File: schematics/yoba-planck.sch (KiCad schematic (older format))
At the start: 106 parts, among them M1 AUDIO-JACK3, M2 AUDIO-JACK3, M3 ARDUINO_PRO_MICRO, Q1 BS170, SW1 SW_PUSH, SW10 SW_PUSH, SW11 SW_PUSH, SW12 SW_PUSH, SW13 SW_PUSH, SW14 SW_PUSH, SW15 SW_PUSH, SW16 SW_PUSH, SW17 SW_PUSH, SW18 SW_PUSH, SW19 SW_PUSH, SW2 SW_PUSH, SW20 SW_PUSH, SW21 SW_PUSH, SW22 SW_PUSH, SW23 SW_PUSH, SW24 SW_PUSH, SW3 SW_PUSH, SW4 SW_PUSH, SW5 SW_PUSH, SW6 SW_PUSH, SW7 SW_PUSH, SW8 SW_PUSH, SW9 SW_PUSH

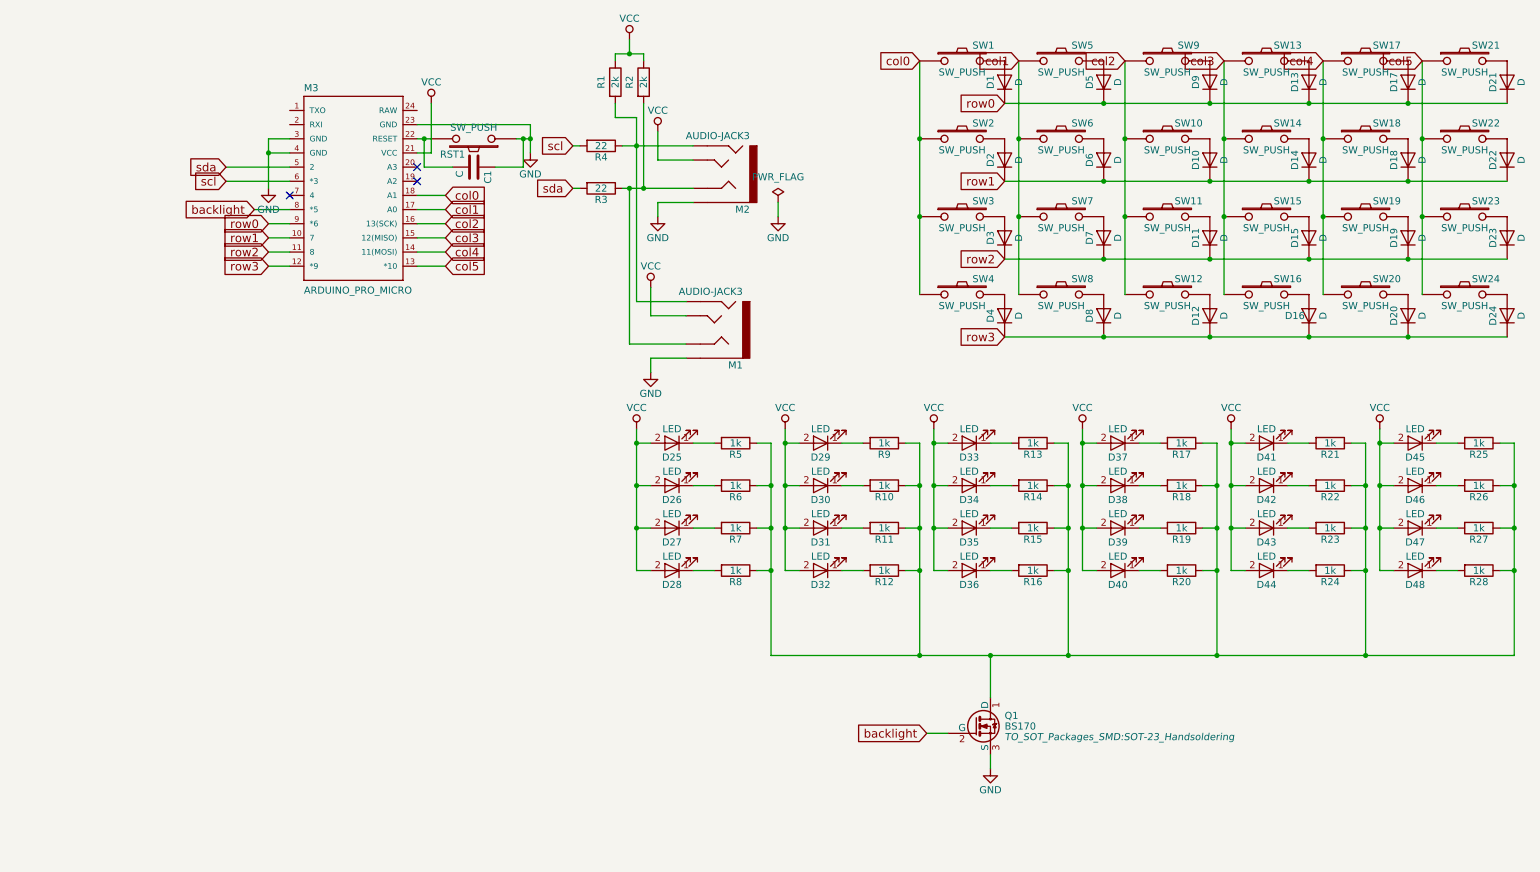
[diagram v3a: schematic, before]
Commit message: yoba rev3 to smd
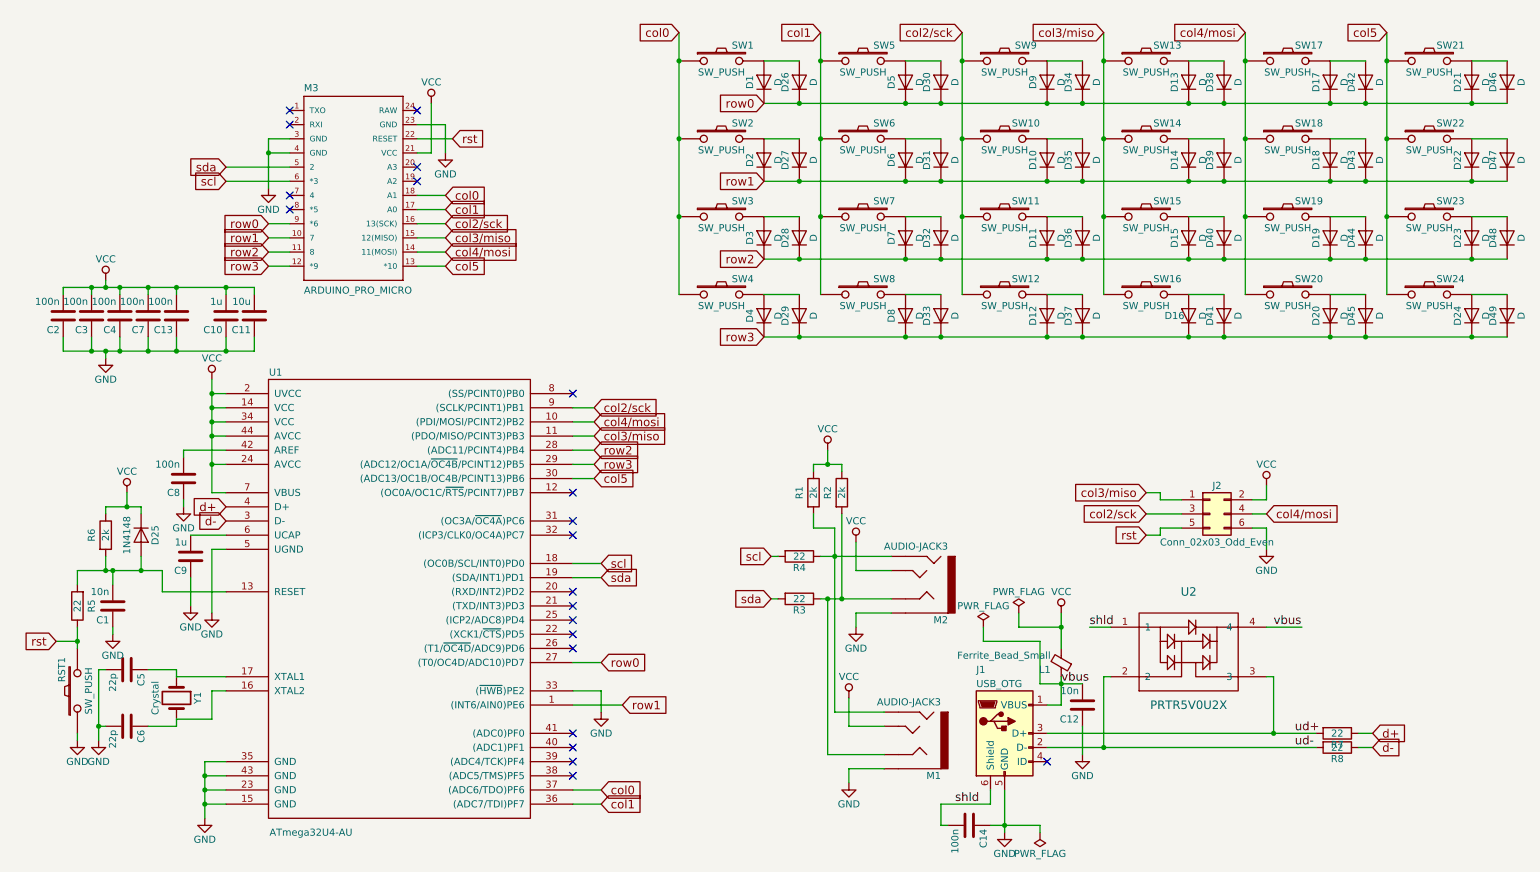
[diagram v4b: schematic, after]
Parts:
- removed D25, D26, D27, D28, D29, D30, D31, D32, D33, D34, D35, D36, D37, D38, D39, D40, D41, D42, D43, D44, D45, D46, D47, D48: LED, mx1a:MX1A-led, symbol LED
- removed Q1: BS170, TO_SOT_Packages_SMD:SOT-23_Handsoldering, symbol BS170
- removed R10, R11, R12, R13, R14, R15, R16, R17, R18, R19, R20, R21, R22, R23, R24, R25, R26, R27, R28, R9: 1k, Resistors_SMD:R_0805_HandSoldering, symbol R
- added C10, C9: 1u, Capacitors_SMD:C_0603_HandSoldering, symbol C
- added C11: 10u, Capacitors_SMD:C_0805_HandSoldering, symbol C
- added C12: 10n, Capacitors_SMD:C_0603_HandSoldering, symbol C
- added C13, C14, C2, C3, C4, C7, C8: 100n, Capacitors_SMD:C_0603_HandSoldering, symbol C
- added C5, C6: 22p, Capacitors_SMD:C_0603_HandSoldering, symbol C
- added D25: 1N4148, Diodes_SMD:SOD-123, symbol D
- added D26, D27, D28, D29, D30, D31, D32, D33, D34, D35, D36, D37, D38, D39, D40, D41, D42, D43, D44, D45, D46, D47, D48, D49: D, Diodes_SMD:SOD-123, symbol D
- added J1: USB_OTG, Connect:USB_Micro-B_10103594-0001LF, symbol USB_OTG
- added J2: Conn_02x03_Odd_Even, Pin_Headers:Pin_Header_Straight_2x03, symbol Conn_02x03_Odd_Even
- added L1: Ferrite_Bead_Small, Capacitors_SMD:C_0603_HandSoldering, symbol Ferrite_Bead_Small
- added U1: ATmega32U4-AU, Housings_QFP:TQFP-44_10x10mm_Pitch0.8mm, symbol ATmega32U4-AU
- added U2: PRTR5V0U2X, yoba:SOT143B, symbol PRTR5V0U2X
- added Y1: Crystal, Crystals:Crystal_SMD_5032_2Pads, symbol Crystal
- C1: value C -> 10n; footprint Capacitors_SMD:C_0805_HandSoldering -> Capacitors_SMD:C_0603_HandSoldering
- R1, R2, R3, R4: footprint Resistors_SMD:R_0805_HandSoldering -> Resistors_Universal:Resistor_SMDuniversal_0805to1206_HandSoldering
- R5, R7, R8: value 1k -> 22; footprint Resistors_SMD:R_0805_HandSoldering -> Resistors_SMD:R_0603_HandSoldering
- R6: value 1k -> 2k; footprint Resistors_SMD:R_0805_HandSoldering -> Resistors_SMD:R_0603_HandSoldering
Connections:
- net GND: now also C10.1, C11.1, C12.1, C13.1, C14.1, C2.1, C3.1, C4.1, C5.2, C6.2, C7.1, C8.1, C9.1, J1.5 (GND), J2.6 (Pin_6), U1.15 (GND), U1.23 (GND), U1.33 ((~HWB~)PE2), U1.35 (GND), U1.43 (GND), U1.5 (UGND)
- net VCC: now also R6.1, C10.2, C11.2, C13.2, C2.2, C3.2, C4.2, C7.2, D25.1 (K), J2.2 (Pin_2), L1.2, U1.14 (VCC), U1.2 (UVCC), U1.24 (AVCC), U1.34 (VCC), U1.44 (AVCC), U1.7 (VBUS)
- net col0: now also U1.37 ((ADC6/TDO)PF6)
- net col1: now also U1.36 ((ADC7/TDI)PF7)
- net col5: now also U1.30 ((ADC13/OC1B/OC4B/PCINT13)PB6)
- net row0: now also D26.1 (K), D30.1 (K), D34.1 (K), D38.1 (K), D42.1 (K), D46.1 (K), U1.27 ((T0/OC4D/ADC10)PD7)
- net row1: now also D27.1 (K), D31.1 (K), D35.1 (K), D39.1 (K), D43.1 (K), D47.1 (K), U1.1 ((INT6/AIN0)PE6)
- net row2: now also D28.1 (K), D32.1 (K), D36.1 (K), D40.1 (K), D44.1 (K), D48.1 (K), U1.28 ((ADC11/PCINT4)PB4)
- net row3: now also D29.1 (K), D33.1 (K), D37.1 (K), D41.1 (K), D45.1 (K), D49.1 (K), U1.29 ((ADC12/OC1A/~OC4B~/PCINT12)PB5)
- net scl: now also U1.18 ((OC0B/SCL/INT0)PD0)
- net sda: now also U1.19 ((SDA/INT1)PD1)
- net at D1.2 (A), SW1.2: now also D26.2 (A)
- net at D5.2 (A), SW5.2: now also D30.2 (A)
- net at D9.2 (A), SW9.2: now also D34.2 (A)
- net at D13.2 (A), SW13.2: now also D38.2 (A)
- net at D17.2 (A), SW17.2: now also D42.2 (A)
- net at D21.2 (A), SW21.2: now also D46.2 (A)
- net at D2.2 (A), SW2.2: now also D27.2 (A)
- net at D6.2 (A), SW6.2: now also D31.2 (A)
- net at D10.2 (A), SW10.2: now also D35.2 (A)
- net at D14.2 (A), SW14.2: now also D39.2 (A)
- net at D18.2 (A), SW18.2: now also D43.2 (A)
- net at D22.2 (A), SW22.2: now also D47.2 (A)
- net at D3.2 (A), SW3.2: now also D28.2 (A)
- net at D7.2 (A), SW7.2: now also D32.2 (A)
- net at D11.2 (A), SW11.2: now also D36.2 (A)
- net at D15.2 (A), SW15.2: now also D40.2 (A)
- net at D19.2 (A), SW19.2: now also D44.2 (A)
- net at D23.2 (A), SW23.2: now also D48.2 (A)
- net at D4.2 (A), SW4.2: now also D29.2 (A)
- net at D8.2 (A), SW8.2: now also D33.2 (A)
- net at D12.2 (A), SW12.2: now also D37.2 (A)
- net at D16.2 (A), SW16.2: now also D41.2 (A)
- net at D20.2 (A), SW20.2: now also D45.2 (A)
- net at D24.2 (A), SW24.2: now also D49.2 (A)
- net rst: now reaches M3.22 (RESET), RST1.2
- net rst: now also R5.1, J2.5 (Pin_5); no longer C1.2
- net at R5.2: now also C1.2, R6.2, D25.2 (A), U1.13 (RESET)
- net ud+: now reaches R7.2
- net ud+: now also J1.3 (D+), U2.3
- net ud-: now reaches R8.2
- net ud-: now also J1.2 (D-), U2.2
- net backlight: no longer names the net of M3.8 (*5)
- net col2 renamed col2/sck
- net col2/sck: now also J2.3 (Pin_3), U1.9 ((SCLK/PCINT1)PB1)
- net col3 renamed col3/miso
- net col3/miso: now also J2.1 (Pin_1), U1.11 ((PDO/MISO/PCINT3)PB3)
- net col4 renamed col4/mosi
- net col4/mosi: now also J2.4 (Pin_4), U1.10 ((PDI/MOSI/PCINT2)PB2)
- new net: C6.1, U1.16 (XTAL2), Y1.2
- new net: C5.1, U1.17 (XTAL1), Y1.1
- new net: C8.2, U1.42 (AREF)
- new net: C9.2, U1.6 (UCAP)
- new net d+: R7.1, U1.4 (D+)
- new net d-: R8.1, U1.3 (D-)
- new net shld: C14.2, J1.6 (Shield), U2.1
- new net vbus: C12.2, J1.1 (VBUS), L1.1, U2.4
- no-connect marks 3 -> 21
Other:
- moved on the sheet: C1, D1, D10, D11, D12, D13, D14, D15, D16, D17, D18, D19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

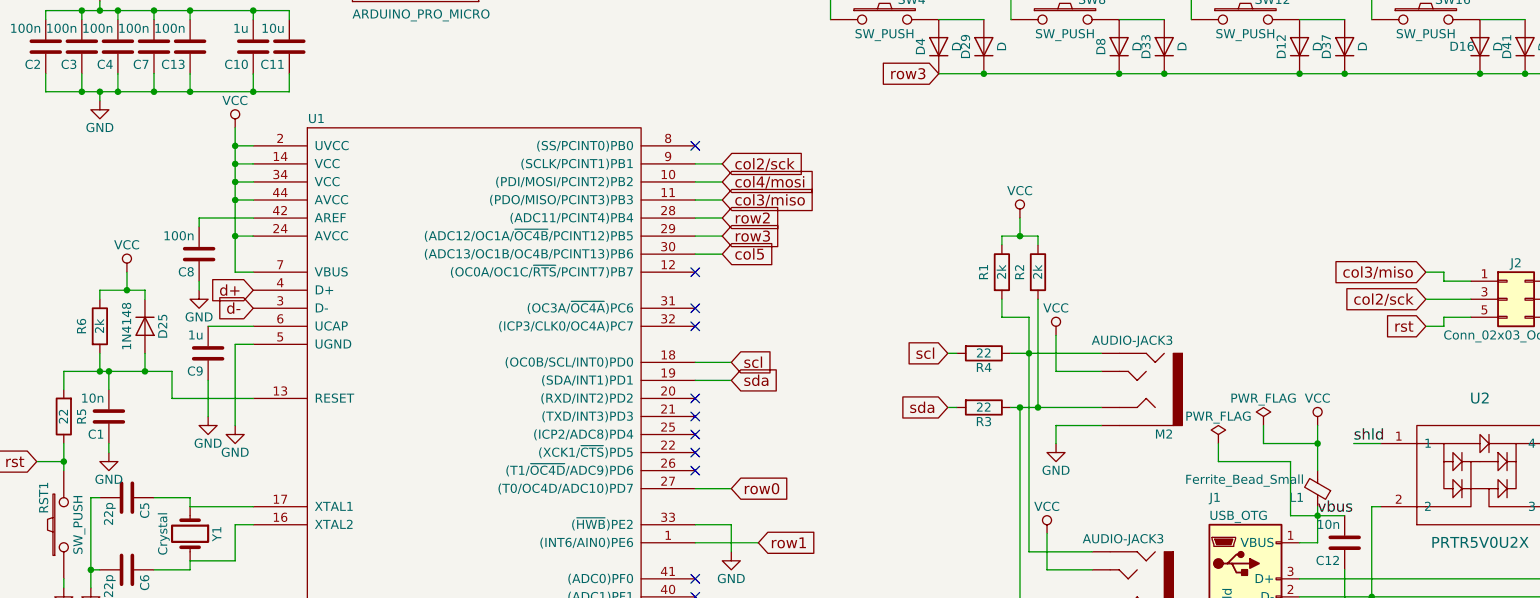
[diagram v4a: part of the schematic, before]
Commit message: fixed vbus sense line for atmega32u4
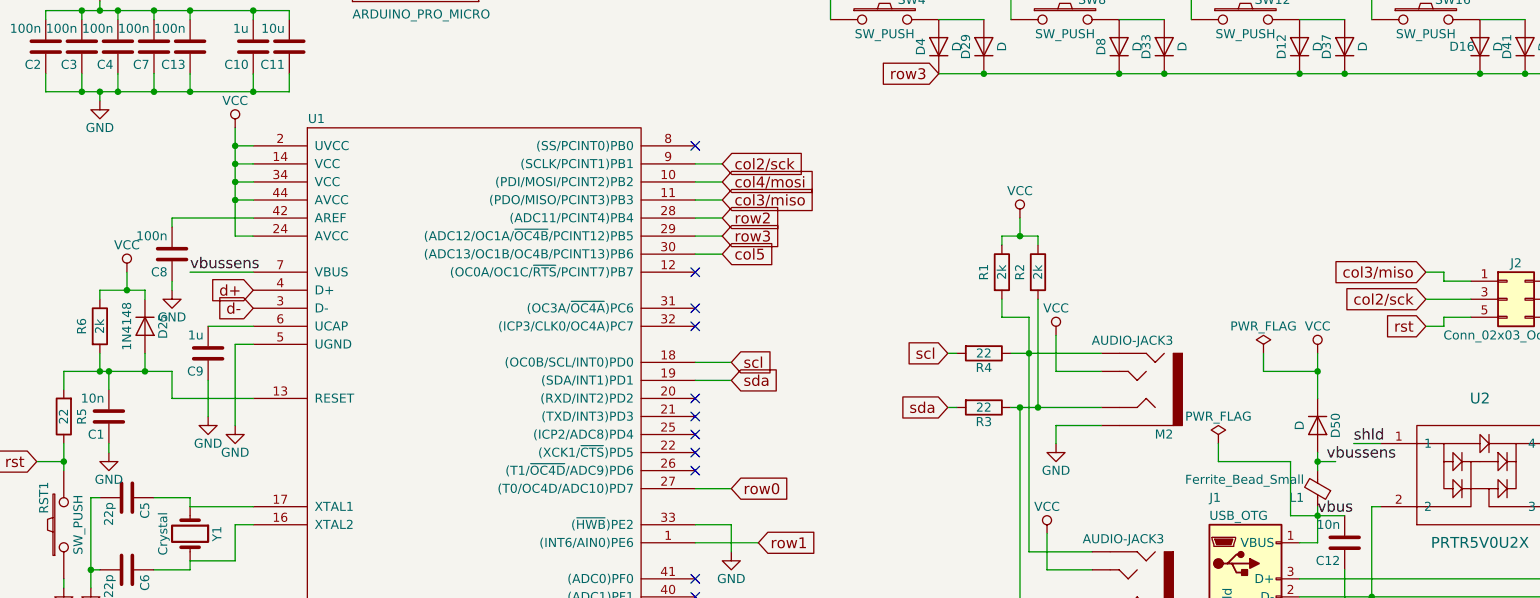
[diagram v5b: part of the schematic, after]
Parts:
- added D50: D, Diodes_SMD:SOD-123, symbol D
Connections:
- net VCC: now also D50.1 (K); no longer L1.2, U1.7 (VBUS)
- new net vbussens: D50.2 (A), L1.2, U1.7 (VBUS)
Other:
- moved on the sheet: C8
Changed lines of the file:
@@
 L C C8
 U 1 1 5A865AB4
-P 1650 3800
-F 0 "C8" H 1675 3900 50  0000 L CNN
-F 1 "100n" H 1675 3700 50  0000 L CNN
-F 2 "Capacitors_SMD:C_0603_HandSoldering" H 1688 3650 50  0001 C CNN
-F 3 "" H 1650 3800 50  0000 C CNN
-	1    1650 3800
+P 1500 3800
+F 0 "C8" H 1525 3900 50  0000 L CNN
+F 1 "100n" H 1525 3700 50  0000 L CNN
+F 2 "Capacitors_SMD:C_0603_HandSoldering" H 1538 3650 50  0001 C CNN
+F 3 "" H 1500 3800 50  0000 C CNN
+	1    1500 3800
 	-1   0    0    1
 $EndComp
@@
 L GND #PWR016
 U 1 1 5A8666E2
-P 1650 4000
-F 0 "#PWR016" H 1650 3750 50  0001 C CNN
-F 1 "GND" H 1650 3850 50  0000 C CNN
-F 2 "" H 1650 4000 50  0000 C CNN
-F 3 "" H 1650 4000 50  0000 C CNN
-	1    1650 4000
+P 1500 4000
+F 0 "#PWR016" H 1500 3750 50  0001 C CNN
+F 1 "GND" H 1500 3850 50  0000 C CNN
+F 2 "" H 1500 4000 50  0000 C CNN
+F 3 "" H 1500 4000 50  0000 C CNN
+	1    1500 4000
 	1    0    0    -1
 $EndComp
@@
 L VCC #PWR021
 U 1 1 5A87C2C3
-P 7850 4750
-F 0 "#PWR021" H 7850 4600 50  0001 C CNN
-F 1 "VCC" H 7850 4900 50  0000 C CNN
-F 2 "" H 7850 4750 50  0000 C CNN
-F 3 "" H 7850 4750 50  0000 C CNN
-	1    7850 4750
+P 7850 4350
+F 0 "#PWR021" H 7850 4200 50  0001 C CNN
+F 1 "VCC" H 7850 4500 50  0000 C CNN
+F 2 "" H 7850 4350 50  0000 C CNN
+F 3 "" H 7850 4350 50  0000 C CNN
+	1    7850 4350
 	1    0    0    -1
 $EndComp
@@
 $EndComp
 $Comp
-L GND #PWR024
+L GND #PWR022
 U 1 1 5A89E415
 P 900 5650
-F 0 "#PWR024" H 900 5400 50  0001 C CNN
+F 0 "#PWR022" H 900 5400 50  0001 C CNN
 F 1 "GND" H 900 5500 50  0000 C CNN
 F 2 "" H 900 5650 50  0000 C CNN
@@
 $EndComp
 $Comp
-L GND #PWR025
+L GND #PWR023
 U 1 1 5A89ED5E
 P 1150 4900
-F 0 "#PWR025" H 1150 4650 50  0001 C CNN
+F 0 "#PWR023" H 1150 4650 50  0001 C CNN
 F 1 "GND" H 1150 4750 50  0000 C CNN
 F 2 "" H 1150 4900 50  0000 C CNN
@@
 NoConn ~ 3300 1200
 $Comp
-L GND #PWR026
+L GND #PWR024
 U 1 1 5A8AA443
 P 3500 1500
-F 0 "#PWR026" H 3500 1250 50  0001 C CNN
+F 0 "#PWR024" H 3500 1250 50  0001 C CNN
 F 1 "GND" H 3500 1350 50  0000 C CNN
 F 2 "" H 3500 1500 50  0000 C CNN
@@
 $EndComp
 $Comp
-L PWR_FLAG #FLG027
+L PWR_FLAG #FLG025
 U 1 1 5A8ABDC2
-P 7550 4750
-F 0 "#FLG027" H 7550 4825 50  0001 C CNN
-F 1 "PWR_FLAG" H 7550 4900 50  0000 C CNN
-F 2 "" H 7550 4750 50  0001 C CNN
-F 3 "" H 7550 4750 50  0001 C CNN
-	1    7550 4750
-	1    0    0    -1
-$EndComp
-$Comp
-L PWR_FLAG #FLG028
+P 7550 4350
+F 0 "#FLG025" H 7550 4425 50  0001 C CNN
+F 1 "PWR_FLAG" H 7550 4500 50  0000 C CNN
+F 2 "" H 7550 4350 50  0001 C CNN
+F 3 "" H 7550 4350 50  0001 C CNN
+	1    7550 4350
+	1    0    0    -1
+$EndComp
+$Comp
+L PWR_FLAG #FLG026
 U 1 1 5A8AD92E
 P 7700 6300
-F 0 "#FLG028" H 7700 6375 50  0001 C CNN
+F 0 "#FLG026" H 7700 6375 50  0001 C CNN
 F 1 "PWR_FLAG" H 7700 6450 50  0000 C CNN
 F 2 "" H 7700 6300 50  0001 C CNN
@@
 	1950 2900 1950 2800
 Wire Wire Line
-	1850 3100 1850 3900
-Wire Wire Line
 	1850 3200 1950 3200
 Wire Wire Line
@@
 Connection ~ 1850 3500
 Wire Wire Line
-	1850 3900 1950 3900
-Connection ~ 1850 3700
-Wire Wire Line
 	1350 4000 1350 4050
 Wire Wire Line
@@
 Connection ~ 1350 4450
 Wire Wire Line
-	1950 3600 1650 3600
-Wire Wire Line
-	1650 3600 1650 3650
-Wire Wire Line
-	1650 4000 1650 3950
+	1500 3600 1950 3600
+Wire Wire Line
+	1500 3600 1500 3650
+Wire Wire Line
+	1500 4000 1500 3950
 Wire Wire Line
 	9300 3850 9300 3950
@@
 	7850 5400 7850 5200
 Wire Wire Line
-	7850 5000 7850 4750
-Wire Wire Line
-	7550 4750 7550 4850
-Wire Wire Line
-	7550 4850 7850 4850
-Connection ~ 7850 4850
+	7850 4600 7850 4350
+Wire Wire Line
+	7550 4350 7550 4450
+Wire Wire Line
+	7550 4450 7850 4450
+Connection ~ 7850 4450
 Wire Wire Line
 	7350 6000 7350 6100
@@
 Connection ~ 7850 5250
 $Comp
-L GND #PWR029
+L GND #PWR027
 U 1 1 5A8B8C04
 P 8000 5750
-F 0 "#PWR029" H 8000 5500 50  0001 C CNN
+F 0 "#PWR027" H 8000 5500 50  0001 C CNN
 F 1 "GND" H 8000 5600 50  0000 C CNN
 F 2 "" H 8000 5750 50  0000 C CNN
@@
 	8000 5750 8000 5550
 $Comp
-L PWR_FLAG #FLG030
+L PWR_FLAG #FLG028
 U 1 1 5A8BB8EA
 P 7300 4850
-F 0 "#FLG030" H 7300 4925 50  0001 C CNN
+F 0 "#FLG028" H 7300 4925 50  0001 C CNN
 F 1 "PWR_FLAG" H 7300 5000 50  0000 C CNN
 F 2 "" H 7300 4850 50  0001 C CNN
@@
 Text Label 9350 4850 0    60   ~ 0
 vbus
+$Comp
+L D D50
+U 1 1 5AC001B8
+P 7850 4750
+F 0 "D50" H 7850 4850 50  0000 C CNN
+F 1 "D" H 7850 4650 50  0000 C CNN
+F 2 "Diodes_SMD:SOD-123" H 7850 4750 50  0001 C CNN
+F 3 "" H 7850 4750 50  0000 C CNN
+	1    7850 4750
+	0    1    1    0
+$EndComp
+Wire Wire Line
+	7850 4900 7850 5000
+Wire Wire Line
+	7850 4950 7950 4950
+Connection ~ 7850 4950
+Text Label 7900 4950 0    60   ~ 0
+vbussens
+Wire Wire Line
+	1850 3100 1850 3700
+Wire Wire Line
+	1600 3900 1950 3900
+Text Label 1600 3900 0    60   ~ 0
+vbussens
 $EndSCHEMATC
